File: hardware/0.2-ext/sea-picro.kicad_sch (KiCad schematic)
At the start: 54 parts, among them J1 USB_C_Receptacle_USB2.0, J2 0.1" x 12, J3 0.1" x 12, J4 D+, J5 D-, J6 0.1" x 5, Q1 2N7002VC-7, Q2 2N7002VC-7, U1 ME6211C33M5G-N, U2 GD25Q64CWIGR, U3 RP2040, Y1 12MHz

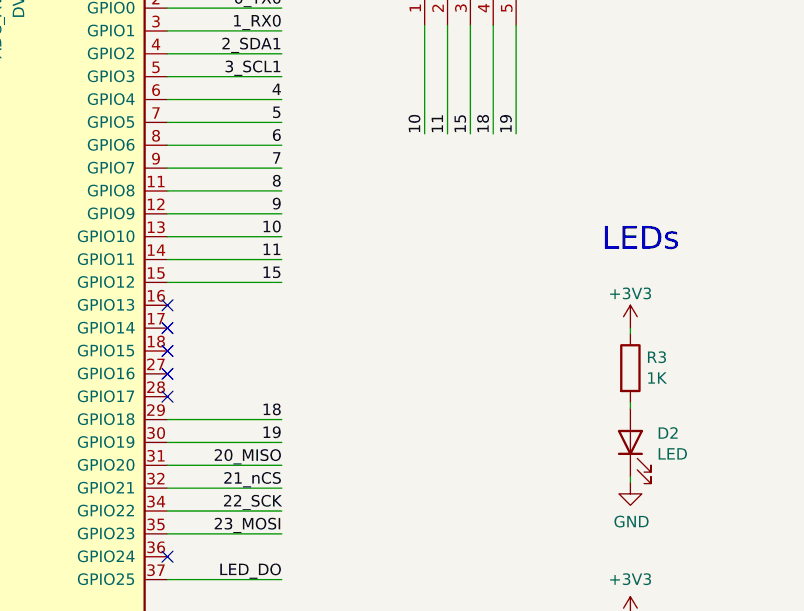
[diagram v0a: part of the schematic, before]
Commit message: add usb vbus detect
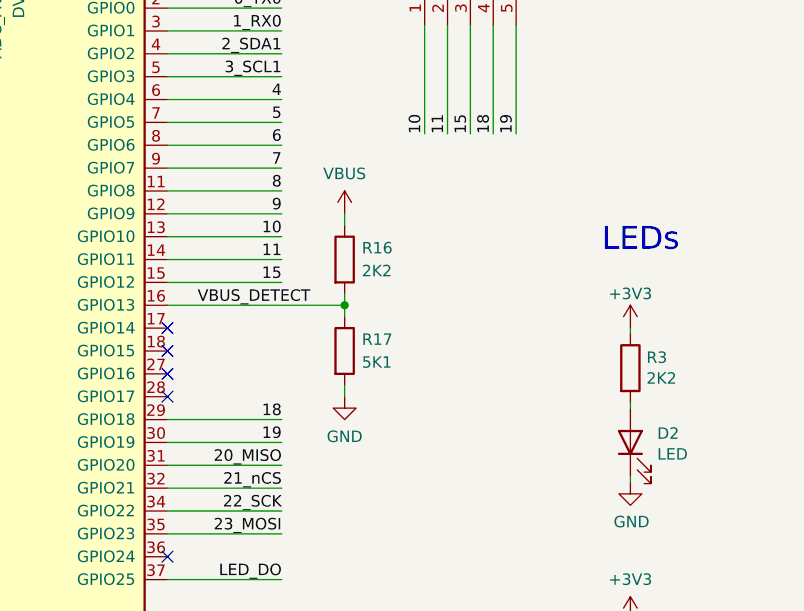
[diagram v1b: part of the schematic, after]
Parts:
- added R16: 2K2, Resistor_SMD:R_0402_1005Metric, symbol Device:R
- added R17: 5K1, Resistor_SMD:R_0402_1005Metric, symbol Device:R
- R3: value 1K -> 2K2; LCSC C11702 -> C25879; MPN  0402WGF1001TCE -> 0402WGF2201TCE
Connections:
- net GND: now also R17.2
- net VBUS: now also R16.1
- net VBUS_DETECT: now reaches U3.16 (GPIO13)
- net VBUS_DETECT: now also R16.2, R17.1
- no-connect marks 7 -> 6
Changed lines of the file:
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@@
   (junction (at 32.385 70.485) (diameter 0) (color 0 0 0 0)
   )
+  (junction (at 234.315 102.235) (diameter 0) (color 0 0 0 0)
+  )
   (junction (at 140.97 106.045) (diameter 0) (color 0 0 0 0)
   )
@@
   (no_connect (at 214.63 130.175))
   (no_connect (at 214.63 107.315))
-  (no_connect (at 214.63 104.775))
-  (no_connect (at 214.63 102.235))
   (no_connect (at 214.63 109.855))
+  (no_connect (at 214.63 104.775))
   (no_connect (at 273.685 146.685))
   (no_connect (at 214.63 112.395))
@@
     (stroke (width 0) (type default) (color 0 0 0 0))
   )
+  (wire (pts (xy 234.315 92.075) (xy 234.315 93.345))
+    (stroke (width 0) (type default) (color 0 0 0 0))
+  )
   (wire (pts (xy 64.77 36.195) (xy 64.77 37.465))
     (stroke (width 0) (type default) (color 0 0 0 0))
@@
     (stroke (width 0) (type default) (color 0 0 0 0))
   )
+  (wire (pts (xy 234.315 111.125) (xy 234.315 112.395))
+    (stroke (width 0) (type default) (color 0 0 0 0))
+  )
   (wire (pts (xy 173.99 191.77) (xy 173.99 190.5))
     (stroke (width 0) (type default) (color 0 0 0 0))
   )
+  (wire (pts (xy 234.315 102.235) (xy 234.315 103.505))
+    (stroke (width 0) (type default) (color 0 0 0 0))
+  )
   (wire (pts (xy 151.765 38.1) (xy 151.765 38.735))
     (stroke (width 0) (type default) (color 0 0 0 0))
@@
     (stroke (width 0) (type default) (color 0 0 0 0))
   )
+  (wire (pts (xy 214.63 102.235) (xy 234.315 102.235))
+    (stroke (width 0) (type default) (color 0 0 0 0))
+  )
   (wire (pts (xy 104.775 31.115) (xy 106.045 31.115))
     (stroke (width 0) (type default) (color 0 0 0 0))
@@
     (stroke (width 0) (type default) (color 0 0 0 0))
   )
+  (wire (pts (xy 234.315 100.965) (xy 234.315 102.235))
+    (stroke (width 0) (type default) (color 0 0 0 0))
+  )
   (wire (pts (xy 214.63 86.995) (xy 227.33 86.995))
     (stroke (width 0) (type default) (color 0 0 0 0))
@@
     (effects (font (size 1.27 1.27)) (justify right bottom))
   )
+  (label "VBUS_DETECT" (at 230.505 102.235 180)
+    (effects (font (size 1.27 1.27)) (justify right bottom))
+  )
   (label "10" (at 243.205 83.185 90)
     (effects (font (size 1.27 1.27)) (justify left bottom))
@@
       (effects (font (size 1.27 1.27)) (justify left))
     )
-    (property "Value" "1K" (id 1) (at 267.843 110.363 0)
+    (property "Value" "2K2" (id 1) (at 267.843 110.363 0)
       (effects (font (size 1.27 1.27)) (justify left))
     )
@@
       (effects (font (size 1.27 1.27)) hide)
     )
-    (property "LCSC" "C11702" (id 4) (at 266.065 109.22 0)
+    (property "LCSC" "C25879" (id 4) (at 266.065 109.22 0)
       (effects (font (size 1.27 1.27)) hide)
     )
-    (property "MPN " "0402WGF1001TCE" (id 5) (at 266.065 109.22 0)
+    (property "MPN " "0402WGF2201TCE" (id 5) (at 266.065 109.22 0)
       (effects (font (size 1.27 1.27)) hide)
     )
@@
     (pin "1")
   )
+  (symbol (lib_id "Device:R") (at 234.315 107.315 0) (unit 1)
+    (in_bom yes) (on_board yes) (fields_autoplaced)
+    (property "Reference" "R17" (id 0) (at 236.22 106.0449 0)
+      (effects (font (size 1.27 1.27)) (justify left))
+    )
+    (property "Value" "5K1" (id 1) (at 236.22 108.5849 0)
+      (effects (font (size 1.27 1.27)) (justify left))
+    )
+    (property "Footprint" "Resistor_SMD:R_0402_1005Metric" (id 2) (at 232.537 107.315 90)
+      (effects (font (size 1.27 1.27)) hide)
+    )
+    (property "Datasheet" "~" (id 3) (at 234.315 107.315 0)
+      (effects (font (size 1.27 1.27)) hide)
+    )
+    (property "JLC Basic" "Y" (id 4) (at 234.315 107.315 0)
+      (effects (font (size 1.27 1.27)) hide)
+    )
+    (property "LCSC" "C25905" (id 5) (at 234.315 107.315 0)
+      (effects (font (size 1.27 1.27)) hide)
+    )
+    (property "MPN " "0402WGF5101TCE" (id 6) (at 234.315 107.315 0)
+      (effects (font (size 1.27 1.27)) hide)
+    )
+    (property "Manufacturer" "UNI-ROYAL(Uniroyal Elec)" (id 7) (at 234.315 107.315 0)
+      (effects (font (size 1.27 1.27)) hide)
+    )
+    (pin "1")
+    (pin "2")
+  )
   (symbol (lib_id "power:+5V") (at 169.545 182.88 0) (unit 1)
     (in_bom yes) (on_board yes)
@@
     (pin "S4")
   )
+  (symbol (lib_id "Device:R") (at 234.315 97.155 0) (unit 1)
+    (in_bom yes) (on_board yes) (fields_autoplaced)
+    (property "Reference" "R16" (id 0) (at 236.22 95.8849 0)
+      (effects (font (size 1.27 1.27)) (justify left))
+    )
+    (property "Value" "2K2" (id 1) (at 236.22 98.4249 0)
+      (effects (font (size 1.27 1.27)) (justify left))
+    )
+    (property "Footprint" "Resistor_SMD:R_0402_1005Metric" (id 2) (at 232.537 97.155 90)
+      (effects (font (size 1.27 1.27)) hide)
+    )
+    (property "Datasheet" "~" (id 3) (at 234.315 97.155 0)
+      (effects (font (size 1.27 1.27)) hide)
+    )
+    (property "JLC Basic" "Y" (id 4) (at 234.315 97.155 0)
+      (effects (font (size 1.27 1.27)) hide)
+    )
+    (property "LCSC" "C25879" (id 5) (at 234.315 97.155 0)
+      (effects (font (size 1.27 1.27)) hide)
+    )
+    (property "MPN " "0402WGF2201TCE" (id 6) (at 234.315 97.155 0)
+      (effects (font (size 1.27 1.27)) hide)
+    )
+    (property "Manufacturer" "UNI-ROYAL(Uniroyal Elec)" (id 7) (at 234.315 97.155 0)
+      (effects (font (size 1.27 1.27)) hide)
+    )
+    (pin "1")
+    (pin "2")
+  )
   (symbol (lib_id "Transistor_FET:FDG6335N") (at 62.865 177.165 270) (mirror x) (unit 2)
     (in_bom yes) (on_board yes)
@@
     (pin "2")
   )
+  (symbol (lib_id "power:VBUS") (at 234.315 92.075 0) (unit 1)
+    (in_bom yes) (on_board yes)
+    (property "Reference" "#PWR0111" (id 0) (at 234.315 95.885 0)
+      (effects (font (size 1.27 1.27)) hide)
+    )
+    (property "Value" "VBUS" (id 1) (at 234.315 87.63 0))
+    (property "Footprint" "" (id 2) (at 234.315 92.075 0)
+      (effects (font (size 1.27 1.27)) hide)
+    )
+    (property "Datasheet" "" (id 3) (at 234.315 92.075 0)
+      (effects (font (size 1.27 1.27)) hide)
+    )
+    (pin "1")
+  )
   (symbol (lib_id "power:+1V1") (at 159.385 70.485 0) (unit 1)
     (in_bom yes) (on_board yes)
@@
     (pin "1")
   )
+  (symbol (lib_id "power:GND") (at 234.315 112.395 0) (unit 1)
+    (in_bom yes) (on_board yes) (fields_autoplaced)
+    (property "Reference" "#PWR0108" (id 0) (at 234.315 118.745 0)
+      (effects (font (size 1.27 1.27)) hide)
+    )
+    (property "Value" "GND" (id 1) (at 234.315 116.84 0))
+    (property "Footprint" "" (id 2) (at 234.315 112.395 0)
+      (effects (font (size 1.27 1.27)) hide)
+    )
+    (property "Datasheet" "" (id 3) (at 234.315 112.395 0)
+      (effects (font (size 1.27 1.27)) hide)
+    )
+    (pin "1")
+  )
   (symbol (lib_id "Connector:Conn_01x01_Male") (at 252.73 28.575 0) (unit 1)
     (in_bom no) (on_board yes) (fields_autoplaced)
@@
       (reference "#PWR0107") (unit 1) (value "+3V3") (footprint "")
     )
+    (path "/813149ca-bf30-400f-a8d2-f23b79a2150b"
+      (reference "#PWR0108") (unit 1) (value "GND") (footprint "")
+    )
     (path "/eee273d2-34e1-49c5-8406-57c0ea9cef7b"
       (reference "#PWR0109") (unit 1) (value "GND") (footprint "")
@@
       (reference "#PWR0110") (unit 1) (value "+3V3") (footprint "")
     )
+    (path "/703ef1f4-76c9-43bd-8eca-aff0ebfc70a3"
+      (reference "#PWR0111") (unit 1) (value "VBUS") (footprint "")
+    )
     (path "/0ebb6172-dcf8-4d0a-bcb0-cc2543a20299"
       (reference "#PWR0112") (unit 1) (value "+5V") (footprint "")
@@
     )
     (path "/00000000-0000-0000-0000-00005e35a0cc"
-      (reference "R3") (unit 1) (value "1K") (footprint "Resistor_SMD:R_0402_1005Metric")
+      (reference "R3") (unit 1) (value "2K2") (footprint "Resistor_SMD:R_0402_1005Metric")
     )
     (path "/43f8a866-9b05-4b81-bed8-22767c4dd6f2"
@@
       (reference "R15") (unit 1) (value "1K") (footprint "Resistor_SMD:R_0402_1005Metric")
     )
+    (path "/19bc7e7e-30d0-4e52-95e6-9bf7de2b568b"
+      (reference "R16") (unit 1) (value "2K2") (footprint "Resistor_SMD:R_0402_1005Metric")
+    )
+    (path "/0b5ec94a-26df-467c-a489-3c8bcd3fe13d"
+      (reference "R17") (unit 1) (value "5K1") (footprint "Resistor_SMD:R_0402_1005Metric")
+    )
     (path "/9d568201-85b4-47a4-8cf6-95aba685d688"

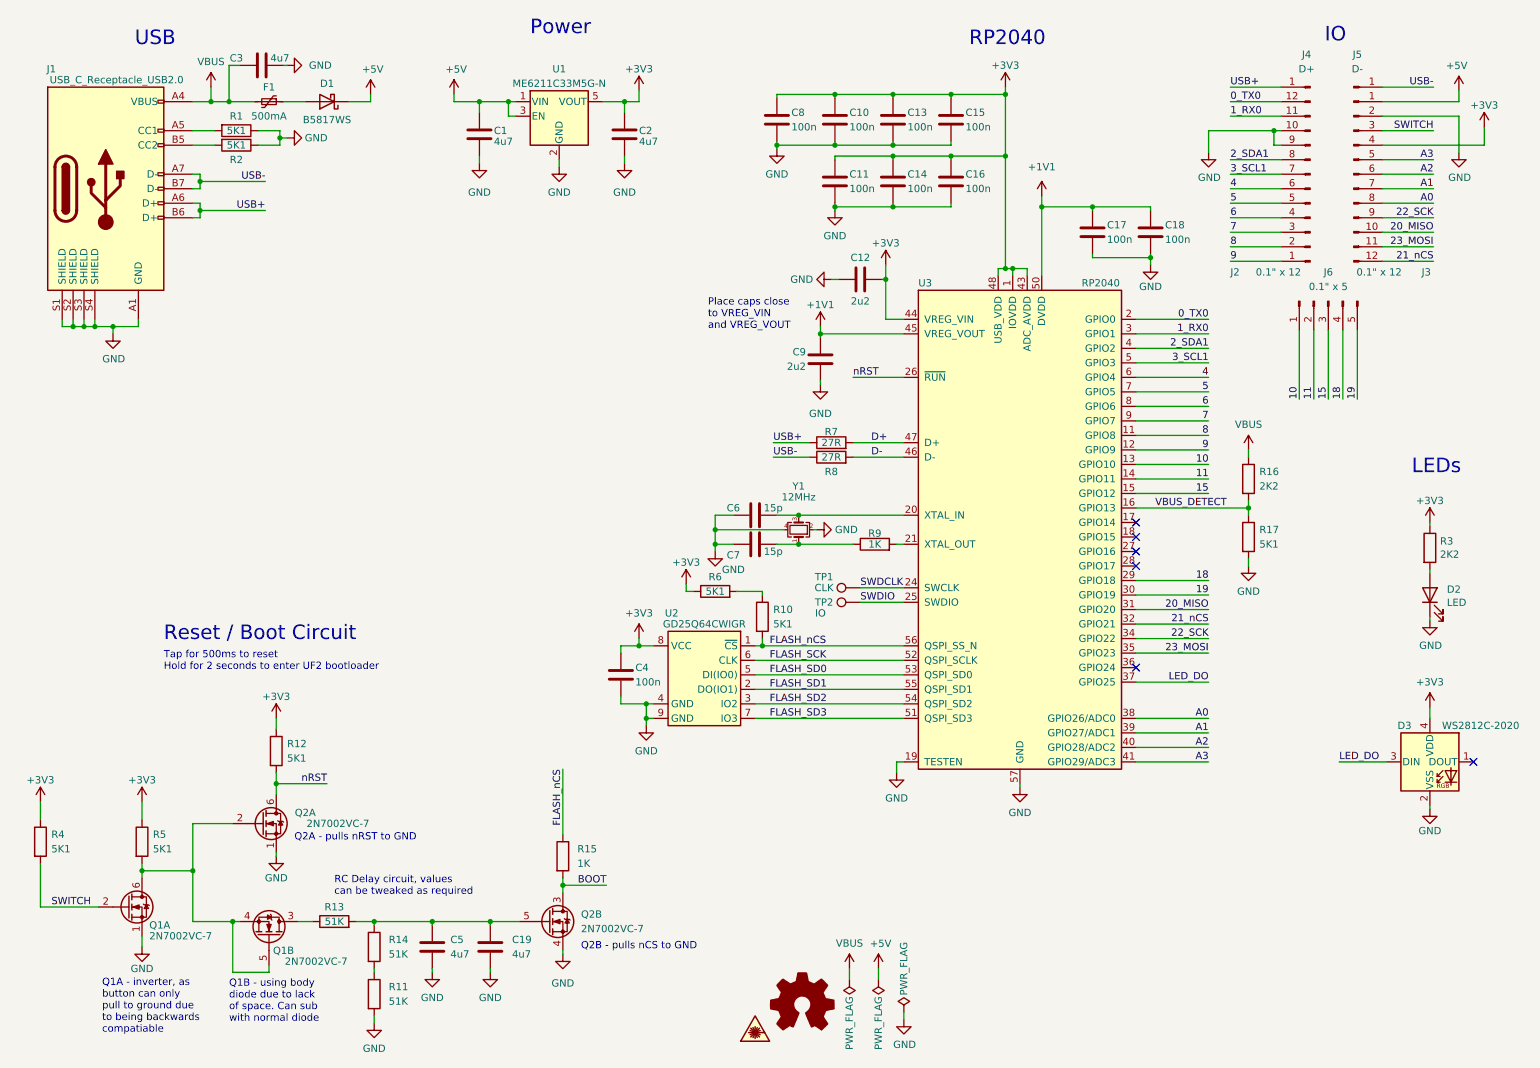
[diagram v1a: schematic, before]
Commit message: add LED driver and more test points
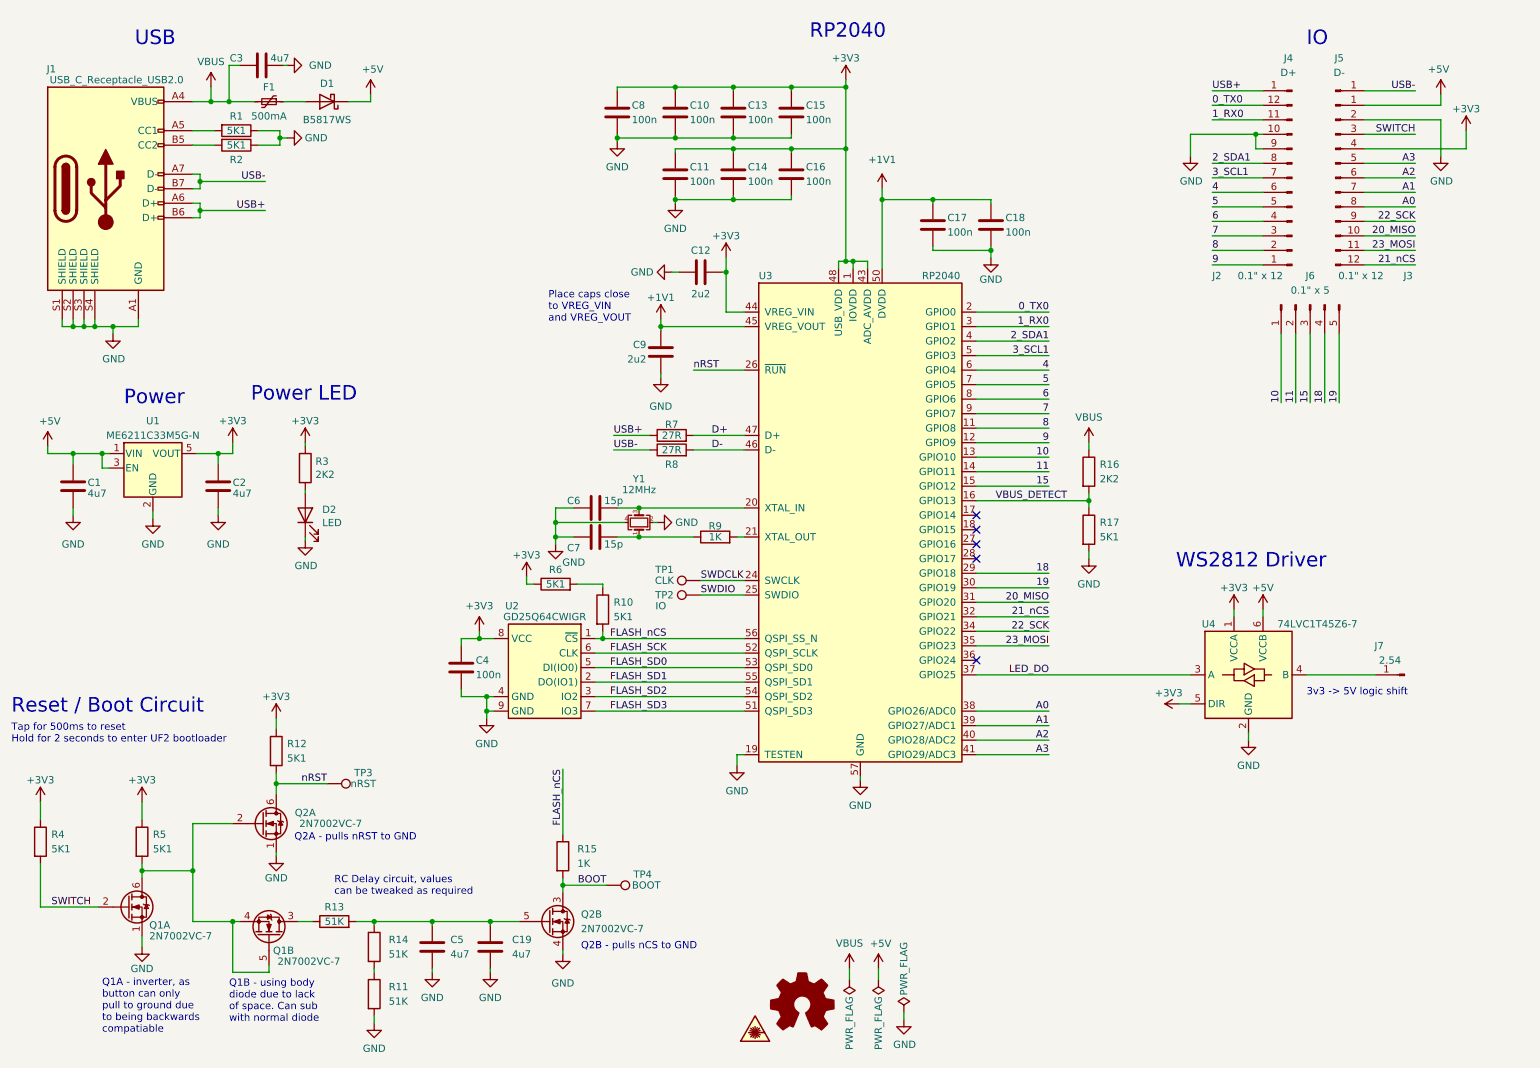
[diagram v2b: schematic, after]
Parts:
- removed D3: WS2812C-2020, josh-led:WS2812C-2020, symbol josh-led:WS2812C-2020
- added J7: 2.54, josh-connectors:PinHeader_1x01_P2.54mm_Circle, symbol Connector:Conn_01x01_Male
- added TP3: nRST, josh-test-point:TestPoint_SMDPad_D1.0mm_NO_SILK, symbol Connector:TestPoint
- added TP4: BOOT, josh-test-point:TestPoint_SMDPad_D1.0mm_NO_SILK, symbol Connector:TestPoint
- added U4: 74LVC1T45Z6-7, Package_TO_SOT_SMD:SOT-563, symbol Logic_LevelTranslator:SN74LVC1T45DRL
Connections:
- net +3V3: now also U4.1 (VCCA), U4.5 (DIR)
- net +5V: now also U4.6 (VCCB)
- net BOOT: now also TP4.1
- net GND: now also U4.2 (GND)
- net LED_DO: now also U4.3 (A)
- net nRST: now also TP3.1
- new net: J7.1 (Pin_1), U4.4 (B)
- no-connect marks 6 -> 5
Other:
- note added: "3v3 -> 5V logic shift"
- note added: "Power LED"
- note added: "WS2812 Driver"
- note removed: "LEDs"
- moved on the sheet: C1, C10, C11, C12, C13, C14, C15, C16, C17, C18, C2, C4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
